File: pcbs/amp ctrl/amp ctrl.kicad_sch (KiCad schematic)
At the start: 60 parts, among them J1 Conn_02x25_Odd_Even, J13 Conn_02x02, J4 Conn_01x02, U10 ADA4004-1, U70 MCP1754ST-3302

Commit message: Amp ctrl: re-arranged connectors
Changed power connector to new (available, better) part number
Moved RJ-45 jacks rightwards (+26 mm X) to leave more room for cable bend radius (fixes #30)
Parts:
- removed H13: #4/M3, MountingHole:MountingHole_3.2mm_M3_Pad_Via, symbol Mechanical:MountingHole_Pad
- J4: footprint shim:Connector_Combo_Molex_386608802_Phoenix_1792229 -> shim:Connector_Phoenix_1190363; MPN (none) -> 1190363; Manufacturer (none) -> Phoenix Contact; Notes Populate choice of either Molex 386608802 (screw) or Phoeni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 -> (none)
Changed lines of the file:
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@@
 			)
 		)
-		(property "Footprint" "shim:Connector_Combo_Molex_386608802_Phoenix_1792229"
+		(property "Footprint" "shim:Connector_Phoenix_1190363"
 			(at 34.29 41.91 0)
 			(hide yes)
@@
 			)
 		)
-		(property "Notes" "Populate choice of either Molex 386608802 (screw) or Phoenix 1792229 (lever spring)"
+		(property "Notes" ""
+			(at 34.29 41.91 0)
+			(hide yes)
+			(show_name no)
+			(do_not_autoplace no)
+			(effects
+				(font
+					(size 1.27 1.27)
+				)
+			)
+		)
+		(property "Manufacturer" "Phoenix Contact"
+			(at 34.29 41.91 0)
+			(hide yes)
+			(show_name no)
+			(do_not_autoplace no)
+			(effects
+				(font
+					(size 1.27 1.27)
+				)
+			)
+		)
+		(property "MPN" "1190363"
 			(at 34.29 41.91 0)
 			(hide yes)
@@
 					(unit 1)
 				)
-			)
-		)
-	)
-	(symbol
-		(lib_id "Mechanical:MountingHole_Pad")
-		(at 54.61 255.27 0)
-		(unit 1)
-		(body_style 1)
-		(exclude_from_sim no)
-		(in_bom no)
-		(on_board yes)
-		(in_pos_files yes)
-		(dnp no)
-		(property "Reference" "H13"
-			(at 57.15 254 0)
-			(show_name no)
-			(do_not_autoplace no)
-			(effects
-				(font
-					(size 1.27 1.27)
-				)
-				(justify left)
-			)
-		)
-		(property "Value" "#4/M3"
-			(at 57.15 256.413 0)
-			(show_name no)
-			(do_not_autoplace no)
-			(effects
-				(font
-					(size 1.27 1.27)
-				)
-				(justify left)
-			)
-		)
-		(property "Footprint" "MountingHole:MountingHole_3.2mm_M3_Pad_Via"
-			(at 54.61 255.27 0)
-			(hide yes)
-			(show_name no)
-			(do_not_autoplace no)
-			(effects
-				(font
-					(size 1.27 1.27)
-				)
-			)
-		)
-		(property "Datasheet" ""
-			(at 54.61 255.27 0)
-			(hide yes)
-			(show_name no)
-			(do_not_autoplace no)
-			(effects
-				(font
-					(size 1.27 1.27)
-				)
-			)
-		)
-		(property "Description" ""
-			(at 54.61 255.27 0)
-			(hide yes)
-			(show_name no)
-			(do_not_autoplace no)
-			(effects
-				(font
-					(size 1.27 1.27)
-				)
-			)
-		)
-		(pin "1"
-		)
-		(instances
-			(project "amp ctrl"
-				(path "/00d85075-94bd-47a5-8ecf-5b7663485c5b"
-					(reference "H13")
-					(unit 1)
-				)
-			)
-		)
-	)
-	(symbol
-		(lib_id "power:GND")
-		(at 54.61 257.81 0)
-		(unit 1)
-		(body_style 1)
-		(exclude_from_sim no)
-		(in_bom yes)
-		(on_board yes)
-		(in_pos_files yes)
-		(dnp no)
-		(property "Reference" "#PWR0618"
-			(at 54.61 264.16 0)
-			(hide yes)
-			(show_name no)
-			(do_not_autoplace no)
-			(effects
-				(font
-					(size 1.27 1.27)
-				)
-			)
-		)
-		(property "Value" "GND"
-			(at 54.737 262.2042 0)
-			(show_name no)
-			(do_not_autoplace no)
-			(effects
-				(font
-					(size 1.27 1.27)
-				)
-			)
-		)
-		(property "Footprint" ""
-			(at 54.61 257.81 0)
-			(hide yes)
-			(show_name no)
-			(do_not_autoplace no)
-			(effects
-				(font
-					(size 1.27 1.27)
-				)
-			)
-		)
-		(property "Datasheet" ""
-			(at 54.61 257.81 0)
-			(hide yes)
-			(show_name no)
-			(do_not_autoplace no)
-			(effects
-				(font
-					(size 1.27 1.27)
-				)
-			)
-		)
-		(property "Description" ""
-			(at 54.61 257.81 0)
-			(hide yes)
-			(show_name no)
-			(do_not_autoplace no)
-			(effects
-				(font
-					(size 1.27 1.27)
-				)
-			)
-		)
-		(pin "1"
-		)
-		(instances
-			(project "amp ctrl"
-				(path "/00d85075-94bd-47a5-8ecf-5b7663485c5b"
-					(reference "#PWR0618")
-					(unit 1)
-				)

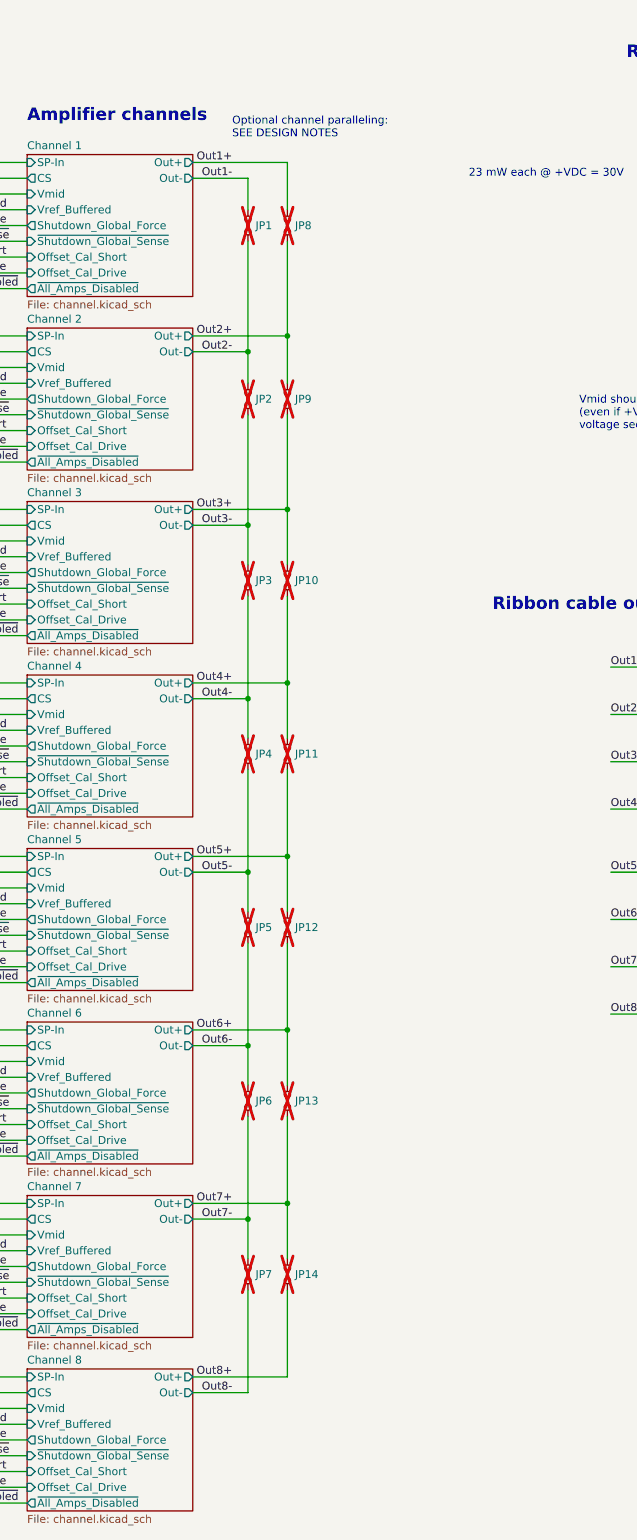
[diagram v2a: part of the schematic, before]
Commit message: Amp ctrl: DAC-filter jumpers, paralleling channels
Added jumpers to disconnect 2nd set of filter capacitors in DAC smoothing filter (fixes #42)
Extended shield footprint around digital section, no longer fits off-the-shelf part (but haven't had a reason to use it yet) to leave room for jumpers
Changed to an experimental channel-paralleling scheme (#19)
Finished copying level shifter layout to other channels (#9)
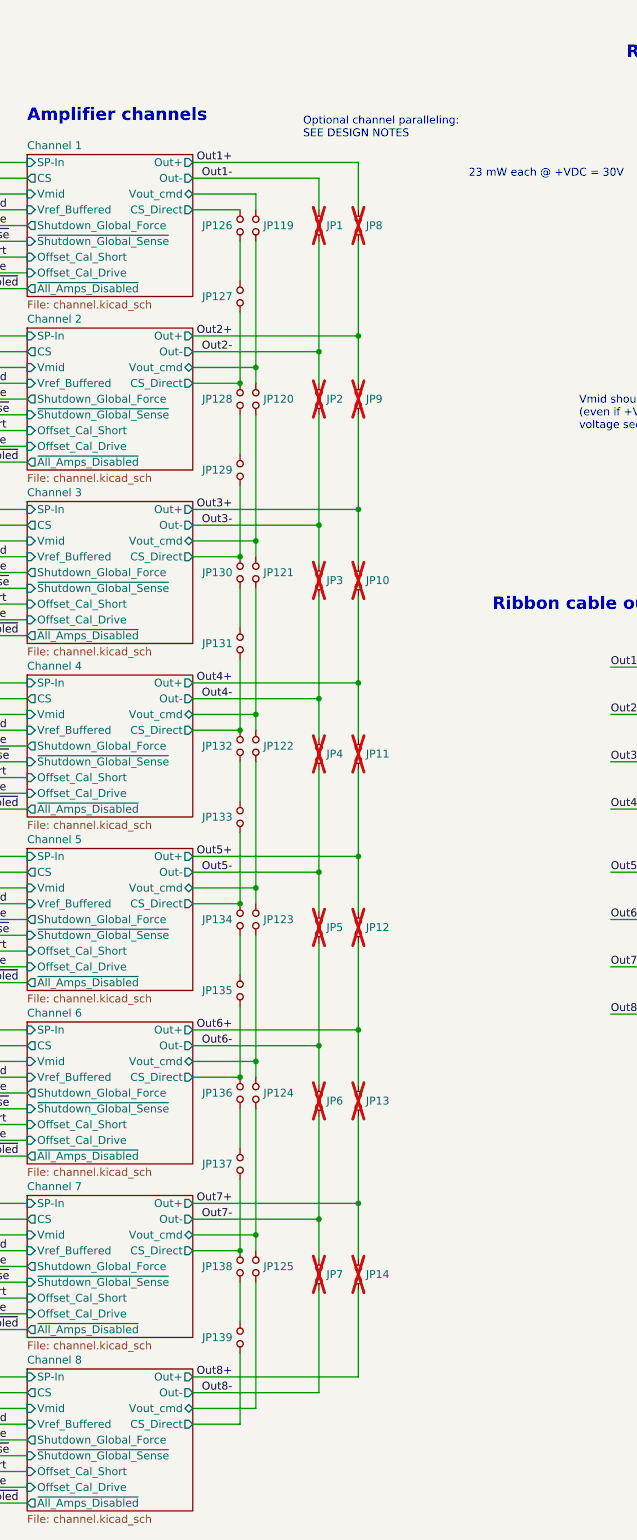
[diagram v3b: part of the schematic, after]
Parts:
- added JP119, JP120, JP121, JP122, JP123, JP124, JP125, JP126, JP127, JP128, JP129, JP130, JP131, JP132, JP133, JP134, JP135, JP136, JP137, JP138, JP139: Jumper_NO_Small, Jumper:SolderJumper-2_P1.3mm_Open_TrianglePad1.0x1.5mm, symbol amp-ctrl-rescue:Jumper_NO_Small-Device
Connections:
- new net: JP126.1, JP127.2
- new net: JP136.1, JP137.2
- new net: JP138.1, JP139.2
- new net: JP130.1, JP131.2
- new net: JP132.1, JP133.2
- new net: JP134.1, JP135.2
- new net: JP128.1, JP129.2
- new net Channel 1/CS_Direct: JP126.2
- new net Channel 1/Vout_cmd: JP119.2
- new net Channel 2/CS_Direct: JP127.1, JP128.2
- new net Channel 2/Vout_cmd: JP119.1, JP120.2
- new net Channel 3/CS_Direct: JP129.1, JP130.2
- new net Channel 3/Vout_cmd: JP120.1, JP121.2
- new net Channel 4/CS_Direct: JP131.1, JP132.2
- new net Channel 4/Vout_cmd: JP121.1, JP122.2
- new net Channel 5/CS_Direct: JP133.1, JP134.2
- new net Channel 5/Vout_cmd: JP122.1, JP123.2
- new net Channel 6/CS_Direct: JP135.1, JP136.2
- new net Channel 6/Vout_cmd: JP123.1, JP124.2
- new net Channel 7/CS_Direct: JP137.1, JP138.2
- new net Channel 7/Vout_cmd: JP124.1, JP125.2
- new net Channel 8/CS_Direct: JP139.1
- new net Channel 8/Vout_cmd: JP125.1
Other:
- sheet Channel 1 ports: added CS_Direct, Vout_cmd; removed none
- sheet Channel 2 ports: added CS_Direct, Vout_cmd; removed none
- sheet Channel 3 ports: added CS_Direct, Vout_cmd; removed none
- sheet Channel 4 ports: added CS_Direct, Vout_cmd; removed none
- sheet Channel 5 ports: added CS_Direct, Vout_cmd; removed none
- sheet Channel 6 ports: added CS_Direct, Vout_cmd; removed none
- sheet Channel 7 ports: added CS_Direct, Vout_cmd; removed none
- sheet Channel 8 ports: added CS_Direct, Vout_cmd; removed none
- moved on the sheet: JP1, JP10, JP11, JP12, JP13, JP14, JP2, JP3, JP4, JP5, JP6, JP7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

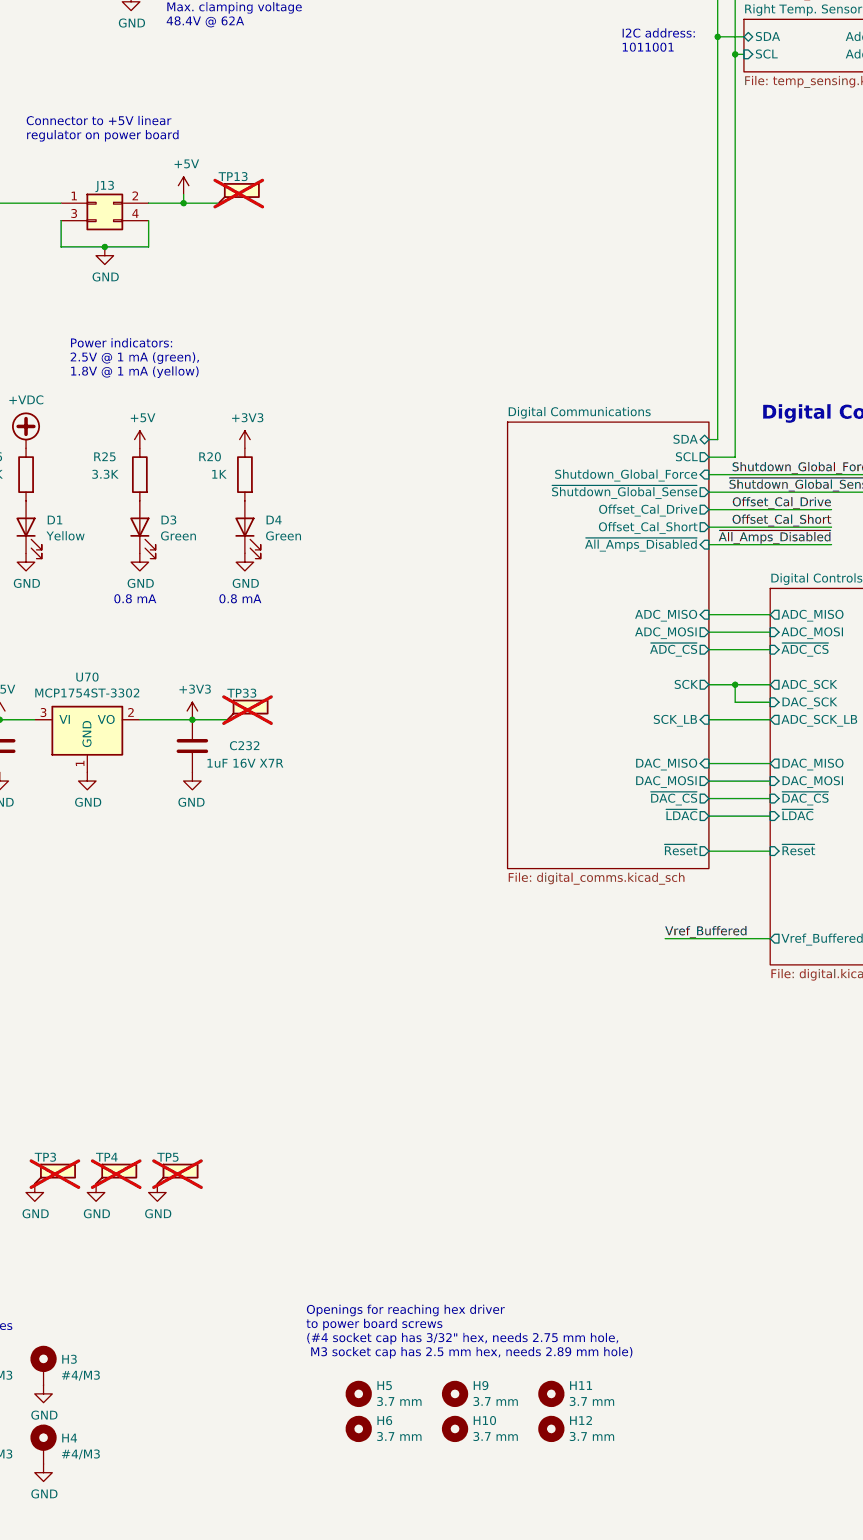
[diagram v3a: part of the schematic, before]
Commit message: Spring connector layout updates
Amp ctrl: added spring connectors for current sense, thermistors, +5V regulator
Amp ctrl: changed pass-through screwdriver holes to mounting holes
Amp ctrl: added part number to optional level shifter
Amp pwr: marked DNP components as DNP
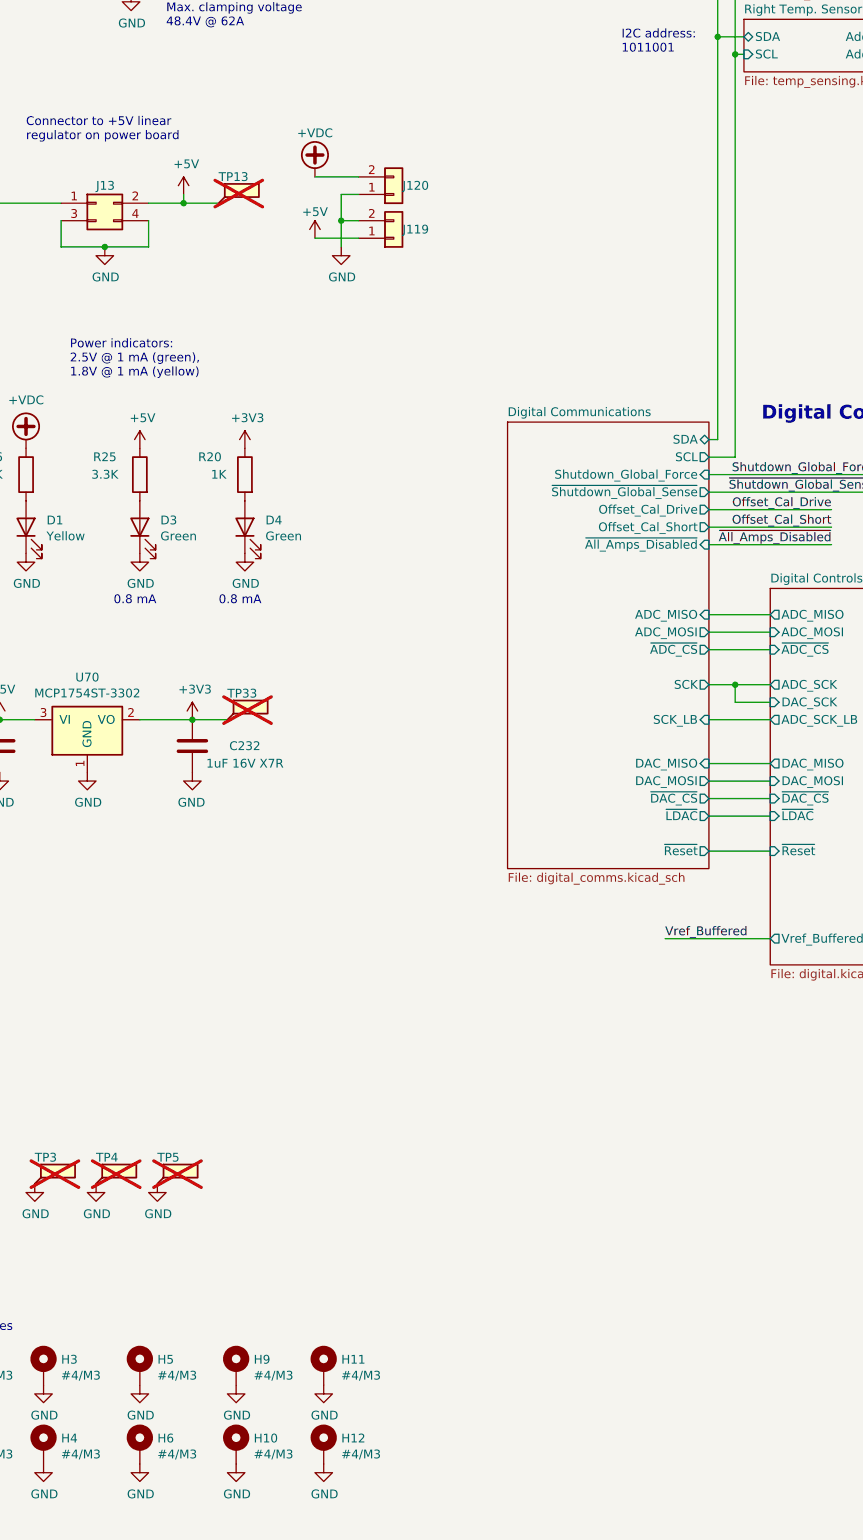
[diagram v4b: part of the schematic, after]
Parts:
- removed H10, H11, H12, H5, H6, H9: 3.7 mm, MountingHole:MountingHole_3.7mm, symbol Mechanical:MountingHole
- added H10, H11, H12, H5, H6, H9: #4/M3, MountingHole:MountingHole_3.2mm_M3_Pad_Via, symbol Mechanical:MountingHole_Pad
- added J119, J120: Conn_01x02, shim:Conn_70AAJ-M_SIB_1x02_P2.54mm_F_bare, symbol Connector_Generic:Conn_01x02
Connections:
- net +5V: now also J119.1 (Pin_1)
- net +VDC: now also J120.2 (Pin_2)
- net GND: now also H10.1, H11.1, H12.1, H5.1, H6.1, H9.1, J119.2 (Pin_2), J120.1 (Pin_1)
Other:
- note removed: "Openings for reaching hex driver to power board screws (#4 socket cap has 3/32" hex, needs 2.75 mm hole, M3 socket cap has 2.5 mm hex, needs 2.89 mm hole)"

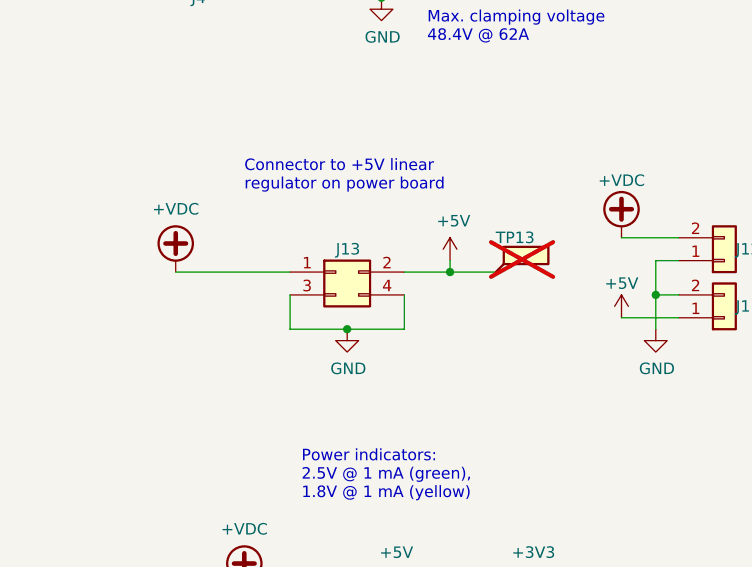
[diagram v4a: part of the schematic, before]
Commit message: Amp ctrl layout for spring pins
Copied layout to all channels & cleaned up inter-channel routing
Updated footprints to latest copies from libraries
Added new SOT-563 footprint for wider clearance between pads, as KiCAD library now has boundary-pushing 0.15 mm (vs. 0.2 mm recc. in 2N7002 datasheet)
Fixed DRC errors
Marked former inter-board connectors (now alternates for spring pins) as DNP
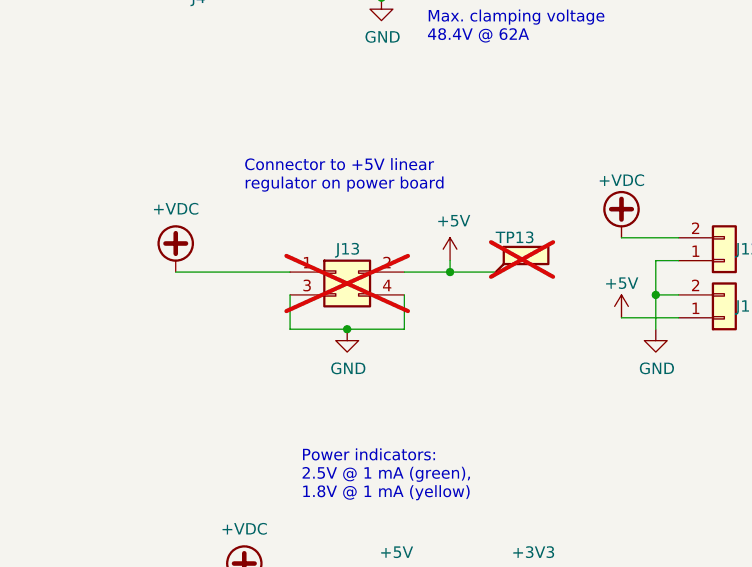
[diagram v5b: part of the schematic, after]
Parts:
- J13: now not fitted
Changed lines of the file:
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@@
 		(on_board yes)
 		(in_pos_files yes)
-		(dnp no)
+		(dnp yes)
 		(property "Reference" "J13"
 			(at 49.53 72.39 0)
@@
 		(in_bom no)
 		(on_board yes)
-		(in_pos_files yes)
+		(in_pos_files no)
 		(dnp no)
 		(property "Reference" "JP74"
@@
 		(in_bom no)
 		(on_board yes)
-		(in_pos_files yes)
+		(in_pos_files no)
 		(dnp no)
 		(property "Reference" "JP75"
@@
 		(in_bom no)
 		(on_board yes)
-		(in_pos_files yes)
+		(in_pos_files no)
 		(dnp no)
 		(property "Reference" "JP77"
@@
 		(in_bom no)
 		(on_board yes)
-		(in_pos_files yes)
+		(in_pos_files no)
 		(dnp no)
 		(property "Reference" "JP78"
@@
 		(in_bom no)
 		(on_board yes)
-		(in_pos_files yes)
+		(in_pos_files no)
 		(dnp no)
 		(property "Reference" "JP79"
@@
 		(in_bom no)
 		(on_board yes)
-		(in_pos_files yes)
+		(in_pos_files no)
 		(dnp no)
 		(property "Reference" "JP80"
